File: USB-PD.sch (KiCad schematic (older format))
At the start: 59 parts, among them IC3 TPS7A0518PDBVT, J1 1053131102, J11 E8124-015-01, Q10 Si7223DN, Q11 Si7223DN, Q12 BSS84AKW, Q14 BSS84AKW, Q9 SQS401EN-T1_BE3, U12 STUSB4500QTR, U14 LTC4418IUF#PBF

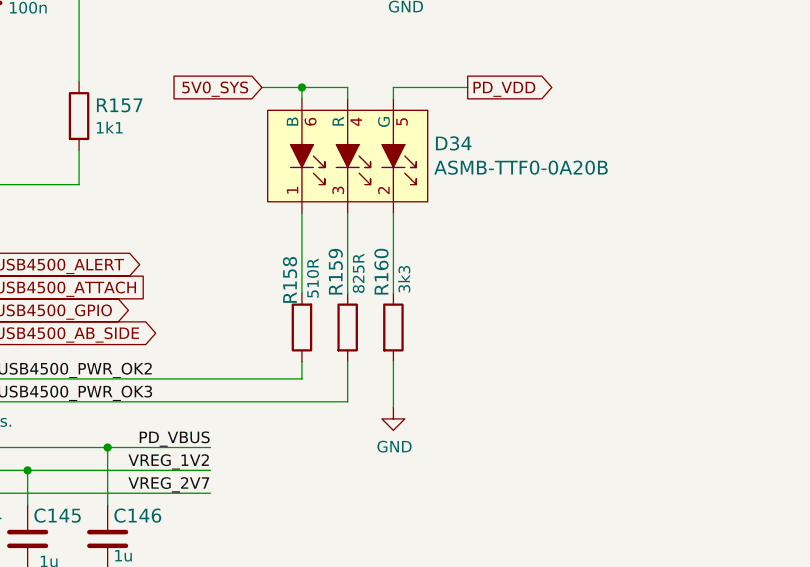
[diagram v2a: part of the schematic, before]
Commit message: Added N-FETs to control USR_LEDs. Reconnected them to 3V3 power supply. Added LED indicating SoM turns on
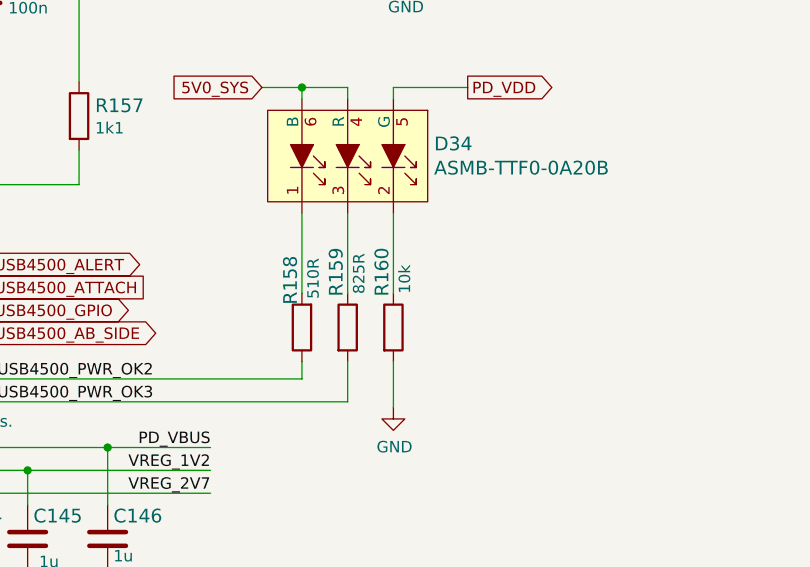
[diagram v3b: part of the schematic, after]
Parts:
- removed R160: R_3k3_0402, sc606-baseboard-footprints:0402-res, symbol sc606-baseboard:R_3k3_0402
- added R160: R_10k_0402, sc606-baseboard-footprints:0402-res, symbol sc606-baseboard:R_10k_0402
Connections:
- net GND: now also R160.2
- net at D34.2: now also R160.1
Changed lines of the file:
@@
 	0    1    1    0
 $EndComp
-$Comp
-L sc606-baseboard:R_3k3_0402 R160
-U 1 1 623007ED
-P 10300 3125
-F 0 "R160" H 9950 3075 60  0000 L CNN
-F 1 "R_3k3_0402" H 10300 2975 60  0001 C CNN
-F 2 "sc606-baseboard-footprints:0402-res" H 10500 3325 60  0001 L CNN
-F 3 "" H 10300 3125 50  0001 C CNN
-F 4 "MULTICOMP PRO" H 10500 3525 60  0001 L CNN "Manufacturer"
-F 5 "MCWR04X3301FTL" H 10500 3425 60  0001 L CNN "MPN"
-F 6 "3k3" H 10025 3175 50  0000 L CNN "Val"
-	1    10300 3125
-	0    1    1    0
-$EndComp
 Wire Wire Line
 	6675 8375 8225 8375
@@
 EndData
 $EndBitmap
+$Comp
+L sc606-baseboard:R_10k_0402 R160
+U 1 1 63040174
+P 10300 3125
+F 0 "R160" H 9950 3075 60  0000 L CNN
+F 1 "R_10k_0402" H 10300 2975 60  0001 C CNN
+F 2 "sc606-baseboard-footprints:0402-res" H 10500 3325 60  0001 L CNN
+F 3 "" H 10300 3125 50  0001 C CNN
+F 4 "VISHAY" H 10500 3525 60  0001 L CNN "Manufacturer"
+F 5 "CRCW040210K0FKEDHP" H 10500 3425 60  0001 L CNN "MPN"
+F 6 "10k" H 10025 3175 50  0000 L CNN "Val"
+	1    10300 3125
+	0    1    1    0
+$EndComp
 $EndSCHEMATC
